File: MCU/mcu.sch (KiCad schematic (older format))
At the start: 5 parts

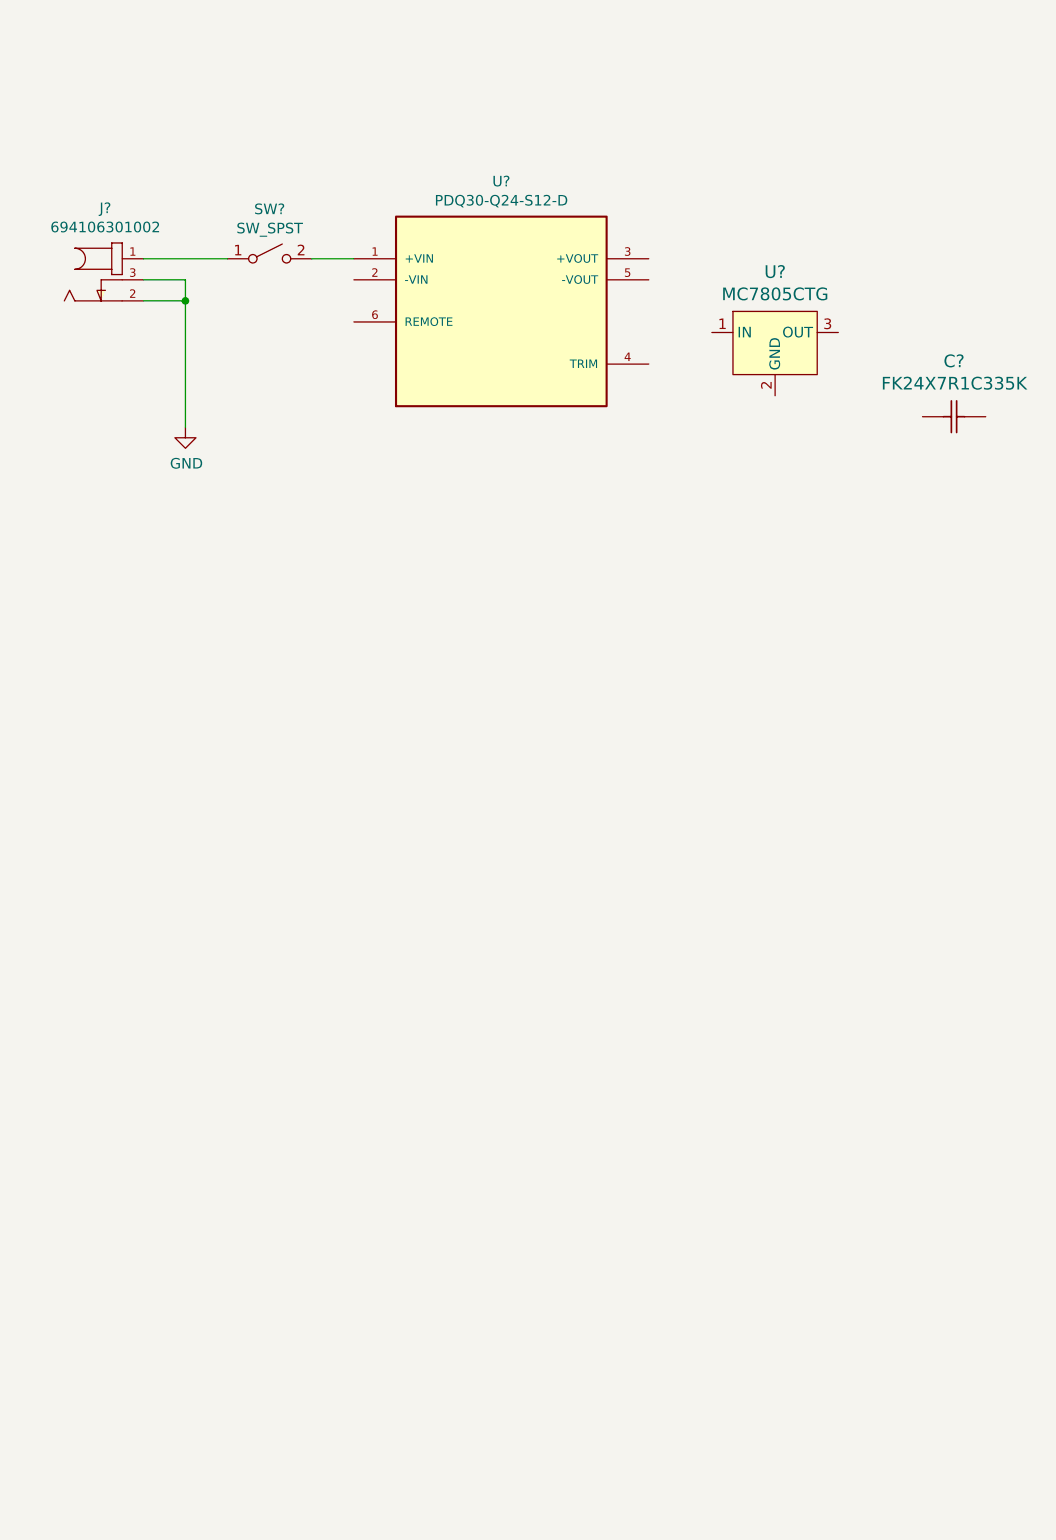
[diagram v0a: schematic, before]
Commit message: MCU: add RPS headers
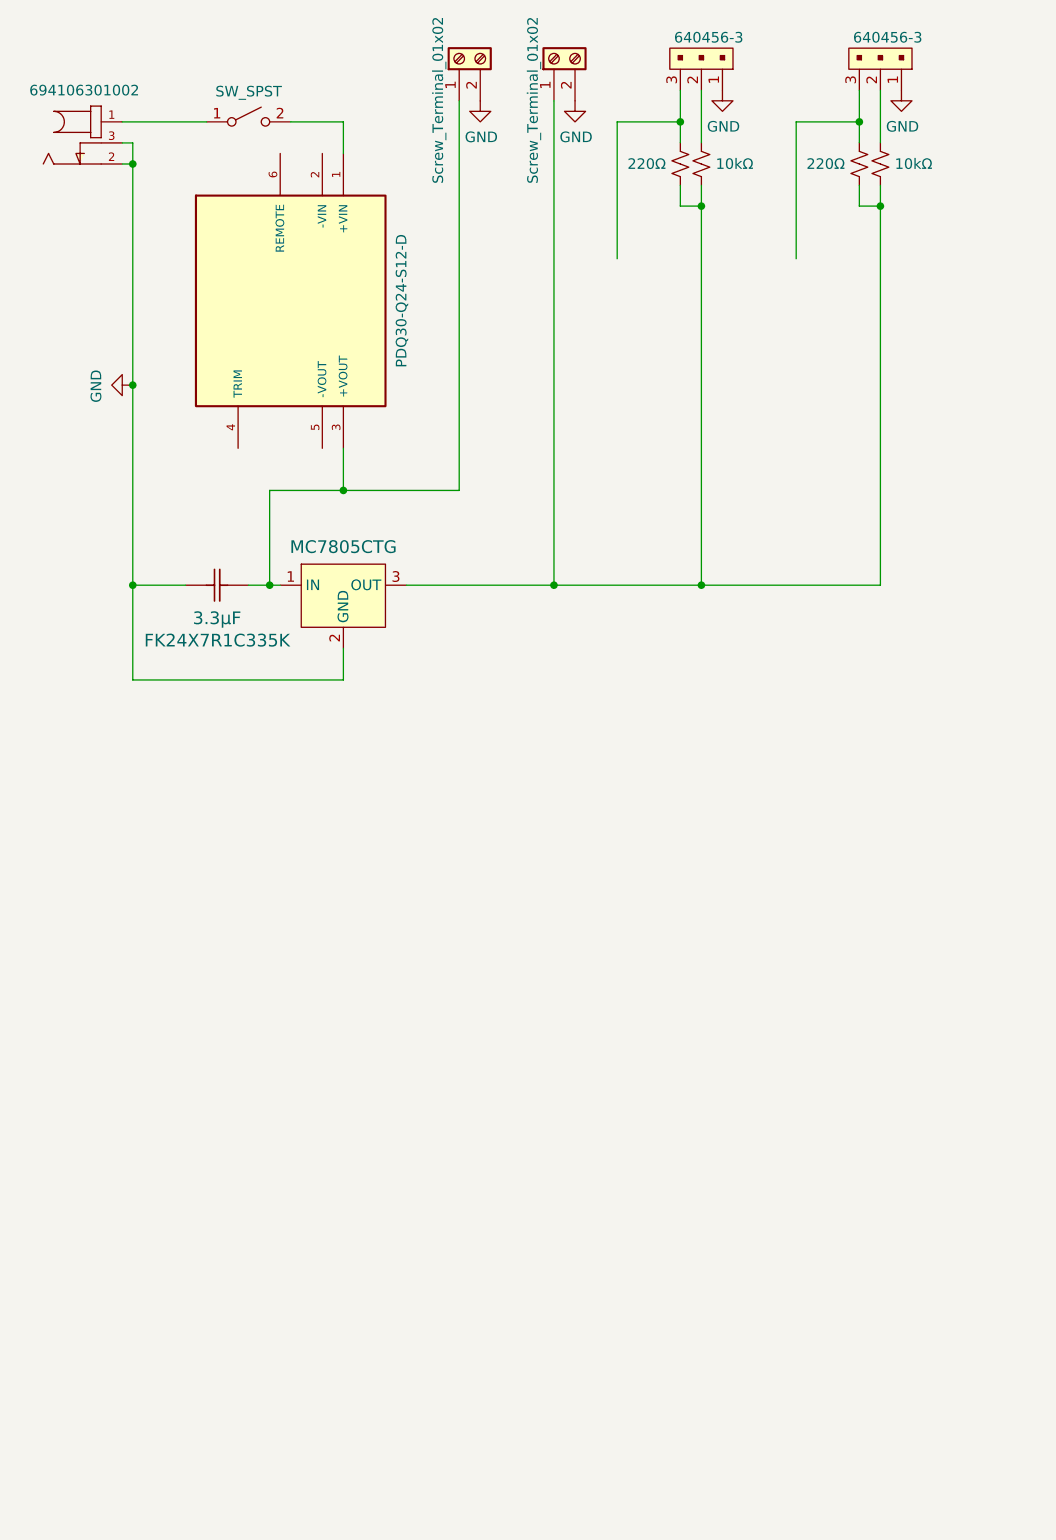
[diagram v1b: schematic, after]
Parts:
- added J? (x2): 640456-3, digikey-footprints:PinHeader_1x3_P2.54_Drill1.1mm, symbol dk_Rectangular-Connectors-Headers-Male-Pins:640456-3
- added J? (x2): Screw_Terminal_01x02, symbol Connector:Screw_Terminal_01x02
- added R? (x2): 10kΩ, symbol Device:R_Small_US
- added R? (x2): 220Ω, symbol Device:R_Small_US
- FK24X7R1C335K: renamed from C?; value FK24X7R1C335K -> 3.3μF
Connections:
- wire segments 6 -> 41
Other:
- moved on the sheet: FK24X7R1C335K

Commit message: add microcontroller
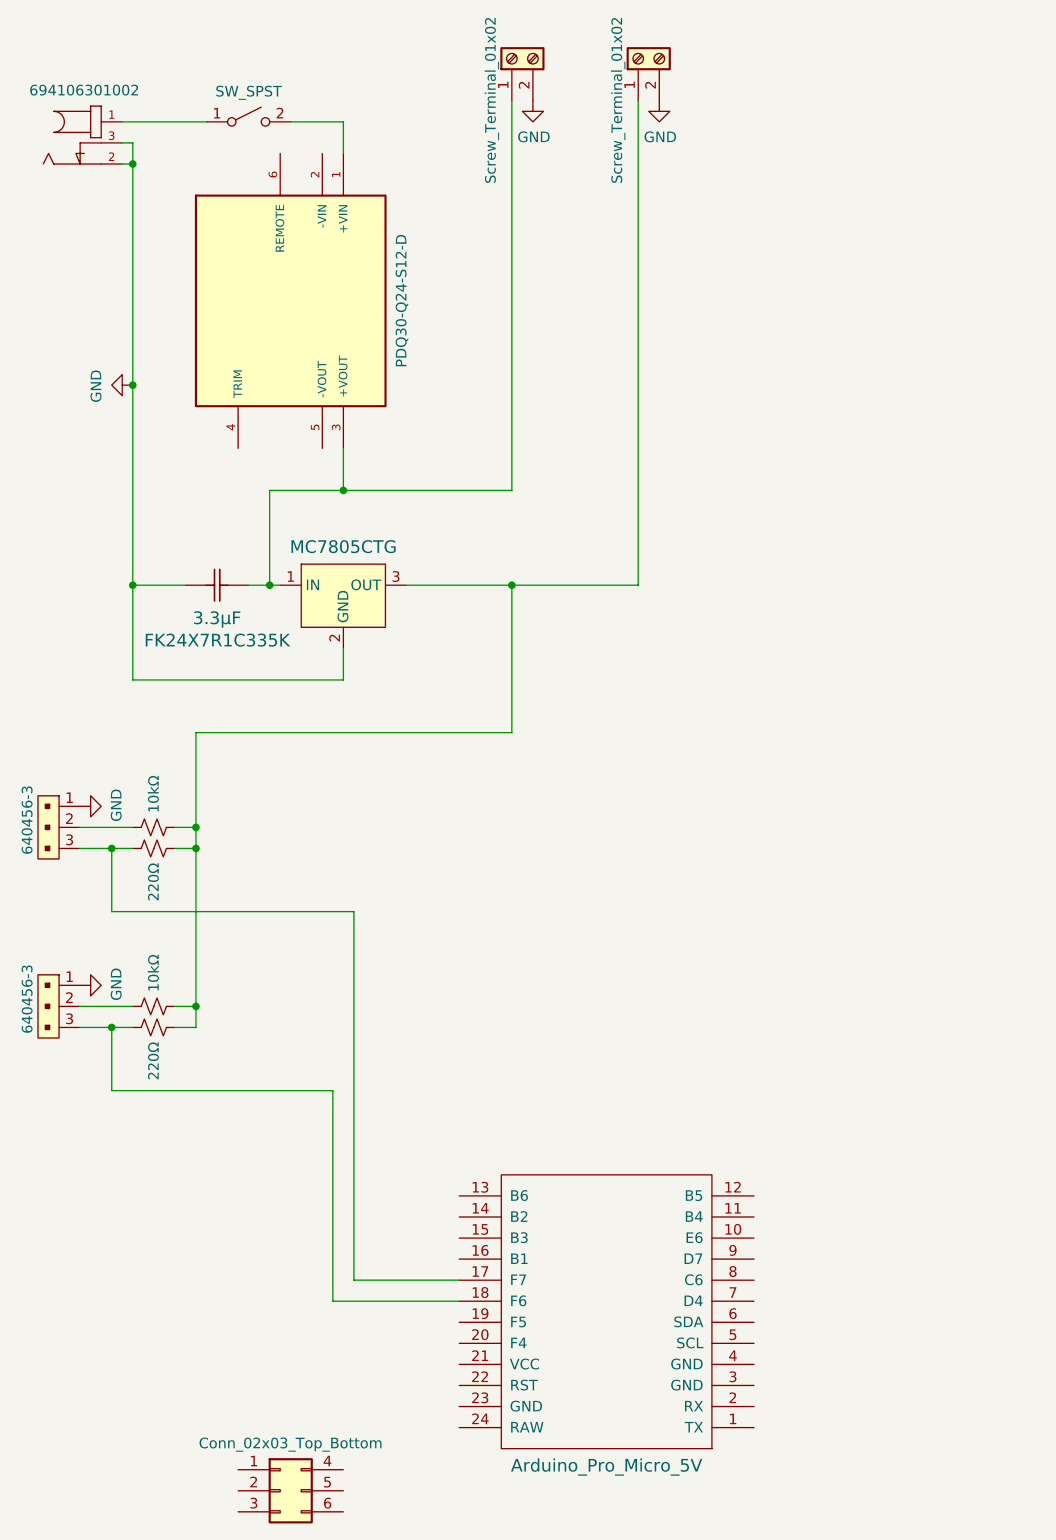
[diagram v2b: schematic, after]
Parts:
- added J?: Conn_02x03_Top_Bottom, symbol Connector_Generic:Conn_02x03_Top_Bottom
- added U?: Arduino_Pro_Micro_5V, symbol promicro:ProMicro
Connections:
- wire segments 41 -> 46
